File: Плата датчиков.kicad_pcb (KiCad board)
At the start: 4 copper layers, 67 x 67 mm, 52 parts, among them J1 A, J10 4900, J11 4900, J12 4900, J13 4900, J14 4900, J15 Conn_02x04_Odd_Even, J2 B, J3 C, J4 4900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

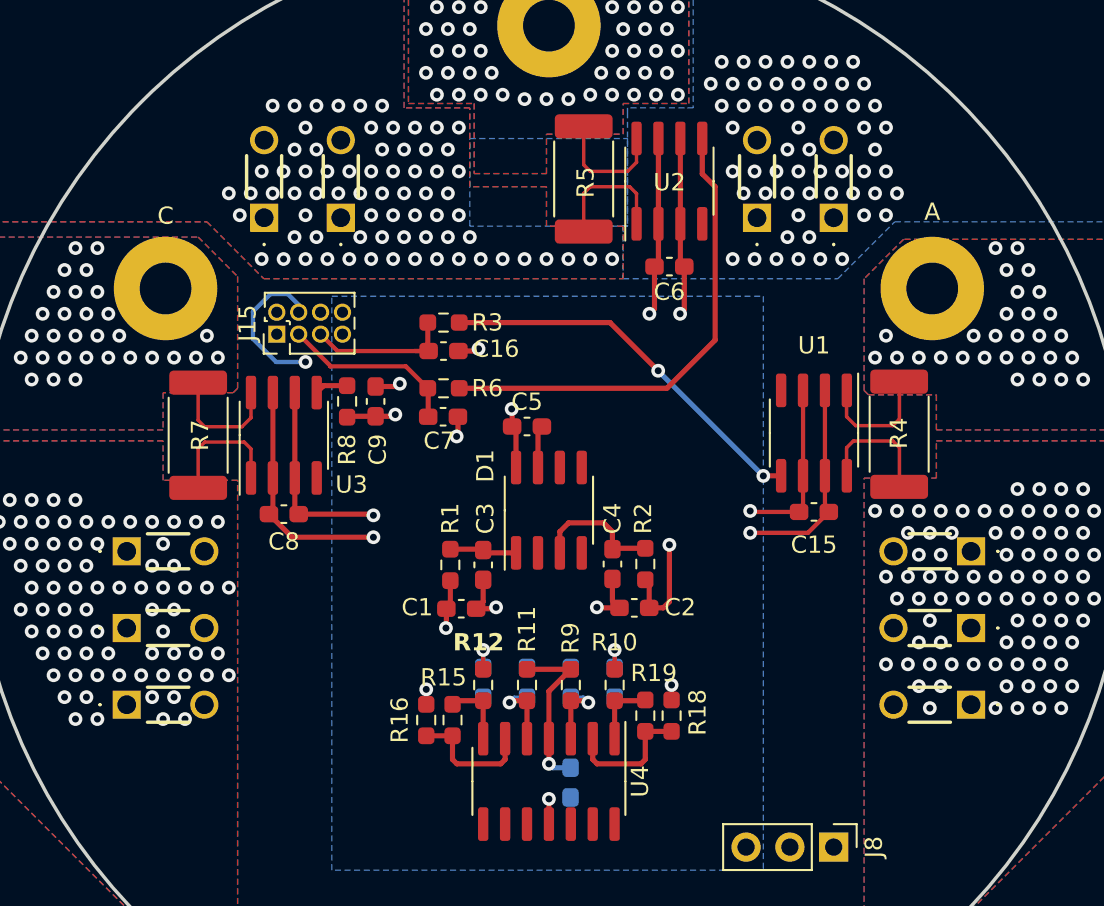
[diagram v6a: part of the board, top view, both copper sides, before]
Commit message: Добавил разъёмы для крепления
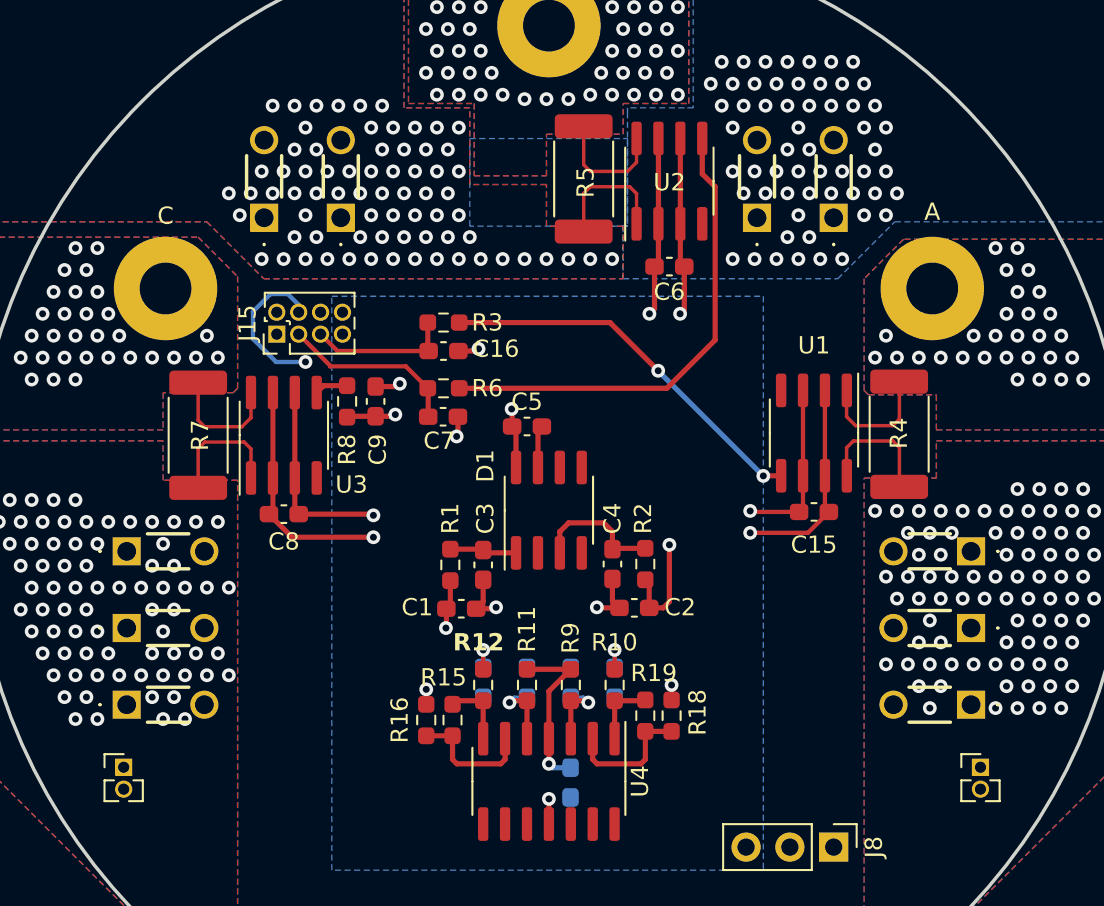
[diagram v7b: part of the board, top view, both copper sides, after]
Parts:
- added J16: Conn_01x02, Connector_PinHeader_1.27mm:PinHeader_1x02_P1.27mm_Vertical, F.Cu at (174.4, 86.0)
- added J17: Conn_01x02, Connector_PinHeader_1.27mm:PinHeader_1x02_P1.27mm_Vertical, F.Cu at (124.7, 86.0)
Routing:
- net Current_A_MCU: track 9.13 -> 8.27 mm

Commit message: Добавил модель плты
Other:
- board size 67 x 67 mm -> 67 x 54.9 mm
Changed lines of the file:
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@@
 		(tags "Through hole pin header THT 1x02 1.27mm single row")
 		(property "Reference" "J16"
-			(at 0 -1.695 360)
+			(at 0 -1.695 0)
 			(layer "F.SilkS")
 			(hide yes)
@@
 		)
 		(property "Value" "Conn_01x02"
-			(at 0 2.965 360)
+			(at 0 2.965 0)
 			(layer "F.Fab")
 			(hide yes)
@@
 		(layer "Dwgs.User")
 	)
-	(gr_circle
-		(center 149.450502 71.074296)
-		(end 182.950502 71.074296)
+	(gr_line
+		(start 175.26 92.456)
+		(end 123.698 92.456)
 		(stroke
-			(width 0.2)
+			(width 0.1)
 			(type default)
 		)
-		(fill none)
 		(layer "Edge.Cuts")
 	)
+	(gr_arc
+		(start 123.698 92.456)
+		(mid 149.479 37.58043)
+		(end 175.26 92.456)
+		(stroke
+			(width 0.1)
+			(type default)
+		)
+		(layer "Edge.Cuts")
+	)
